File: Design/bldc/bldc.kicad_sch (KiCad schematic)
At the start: 0 parts

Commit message: Adding additional pages
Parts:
- added J?: PHASE_C, symbol Connector:Conn_01x01_Male
- added J?: HALL/Encoder, symbol Connector_Generic:Conn_01x06
- added J?: VBATT, symbol Connector:Conn_01x01_Male
- added J?: PHASE_B, symbol Connector:Conn_01x01_Male
- added J?: GND, symbol Connector:Conn_01x01_Male
- added J?: PHASE_A, symbol Connector:Conn_01x01_Male
- added J?: CAN, symbol Connector:DB9_Female_MountingHoles
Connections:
- new net +5V: J?.1 (Pin_1)
- new net +BATT: J?.1 (Pin_1)
- new net GND: J?.0 (PAD), J?.1, J?.1 (Pin_1), J?.3, J?.4, J?.5, J?.6, J?.6 (Pin_6), J?.8, J?.9
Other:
- added sheet CAN Bus Transceiver (CAN.kicad_sch)
- added sheet Filters (hall_filters.kicad_sch)
- added sheet Gate Drivers (gate_drivers.kicad_sch)
- added sheet MCU (STM32F4.kicad_sch)
- added sheet Power MOSFETS (mosfets.kicad_sch)
- note added: "Voltage supply (8V - 20V)"
- title: bldc controller -> BLDC motor controller

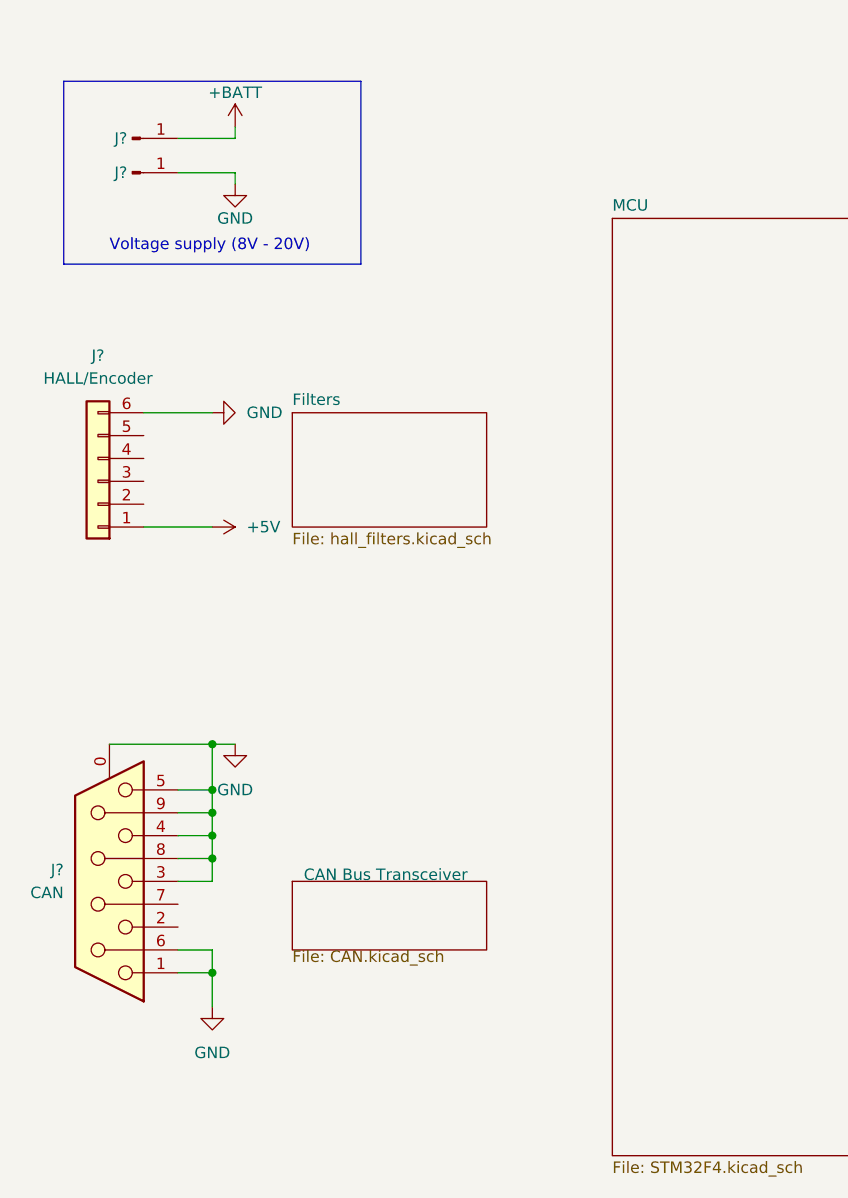
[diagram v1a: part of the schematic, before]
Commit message: Adding components to schematic
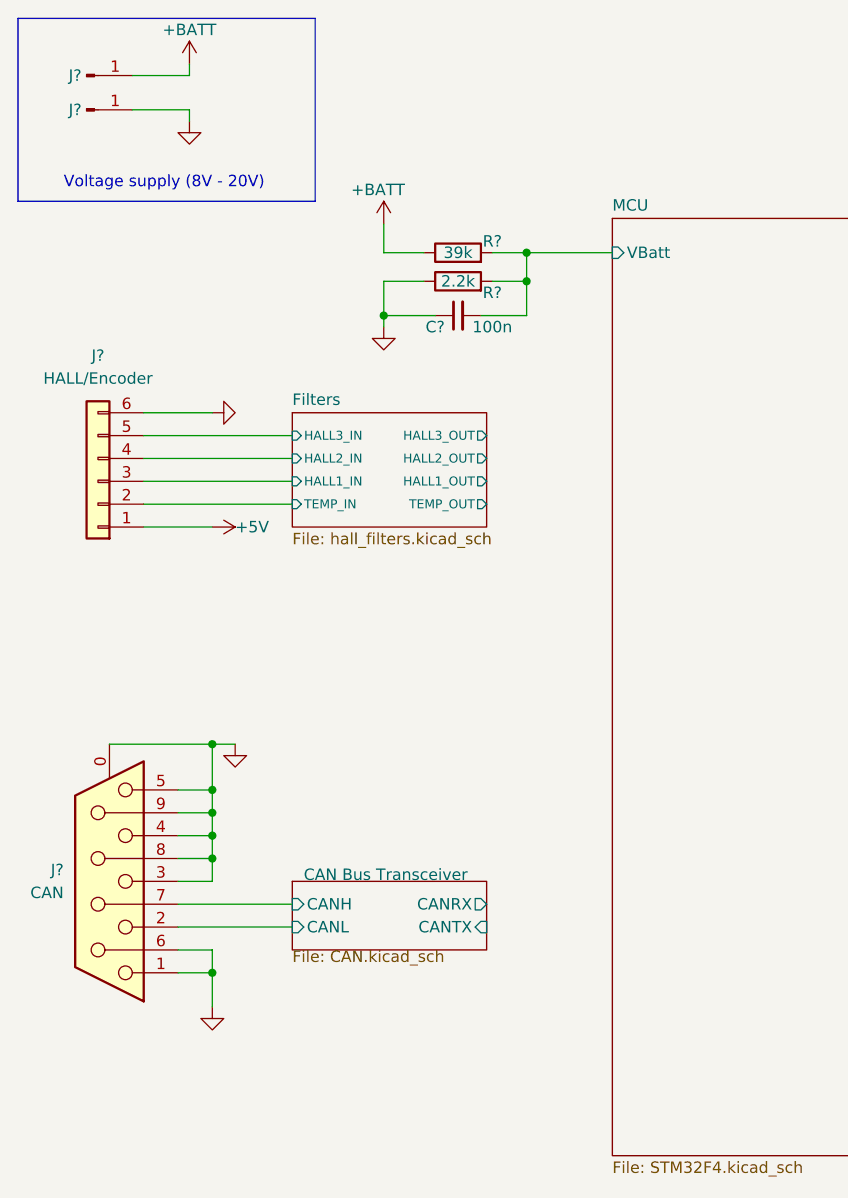
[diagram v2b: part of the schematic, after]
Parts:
- added C?: 100n, symbol Device:C_Small
- added R?: 39k, symbol Device:R
- added R?: 2.2k, symbol Device:R
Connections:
- net +BATT: now also R?.1
- net GND: now also C?.1, R?.1
- net Filters/TEMP_IN: now reaches J?.2 (Pin_2)
- net Filters/HALL1_IN: now reaches J?.3 (Pin_3)
- net Filters/HALL2_IN: now reaches J?.4 (Pin_4)
- net Filters/HALL3_IN: now reaches J?.5 (Pin_5)
- net CAN Bus Transceiver/CANL: now reaches J?.2
- net CAN Bus Transceiver/CANH: now reaches J?.7
- new net MCU/VBatt: C?.2, R?.2, R?.2
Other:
- sheet CAN Bus Transceiver ports: added CANH, CANL, CANRX, CANTX; removed none
- sheet Filters ports: added HALL1_IN, HALL1_OUT, HALL2_IN, HALL2_OUT, HALL3_IN, HALL3_OUT, TEMP_IN, TEMP_OUT; removed none
- sheet MCU ports: added VBatt; removed none
- moved on the sheet: J?
